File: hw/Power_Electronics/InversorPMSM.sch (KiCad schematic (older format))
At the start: 101 parts, among them J1 FROM_CONTROL_BOARD, Q1 HY1908D, Q10 JCS24N50WH, Q11 JCS24N50WH, Q12 JCS24N50WH, Q2 HY1908D, Q3 HY1908D, Q4 HY1908D, Q5 HY1908D, Q6 HY1908D, Q7 JCS24N50WH, Q8 JCS24N50WH, Q9 JCS24N50WH, U1 STDRIVE601

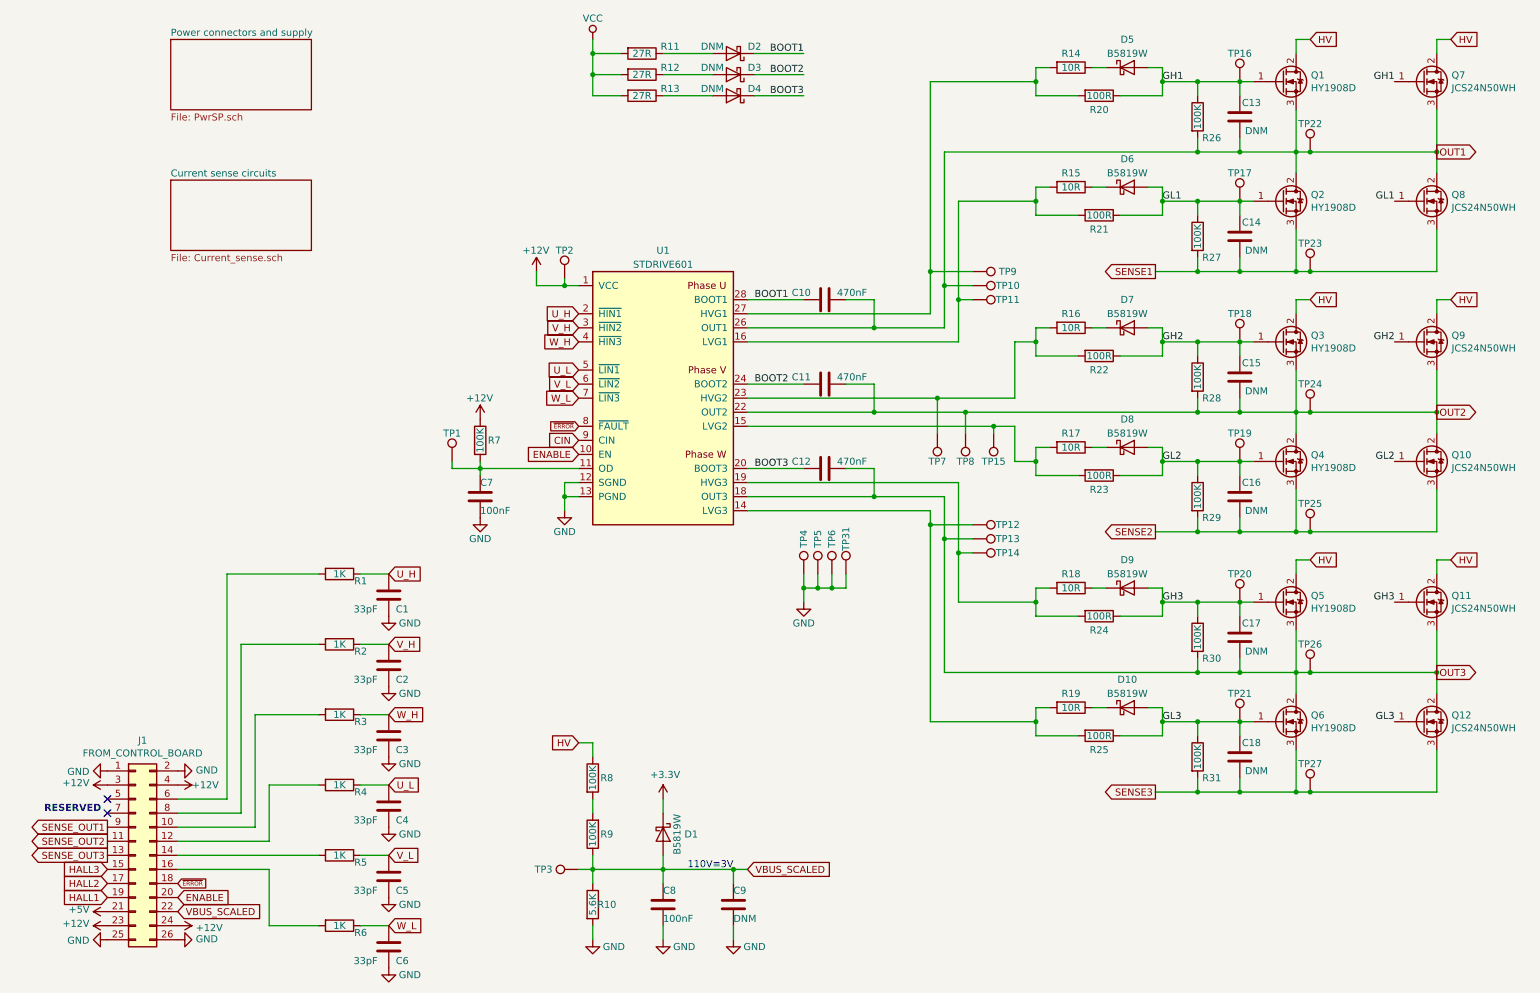
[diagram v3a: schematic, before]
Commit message: adjustments made on silkscreen layer
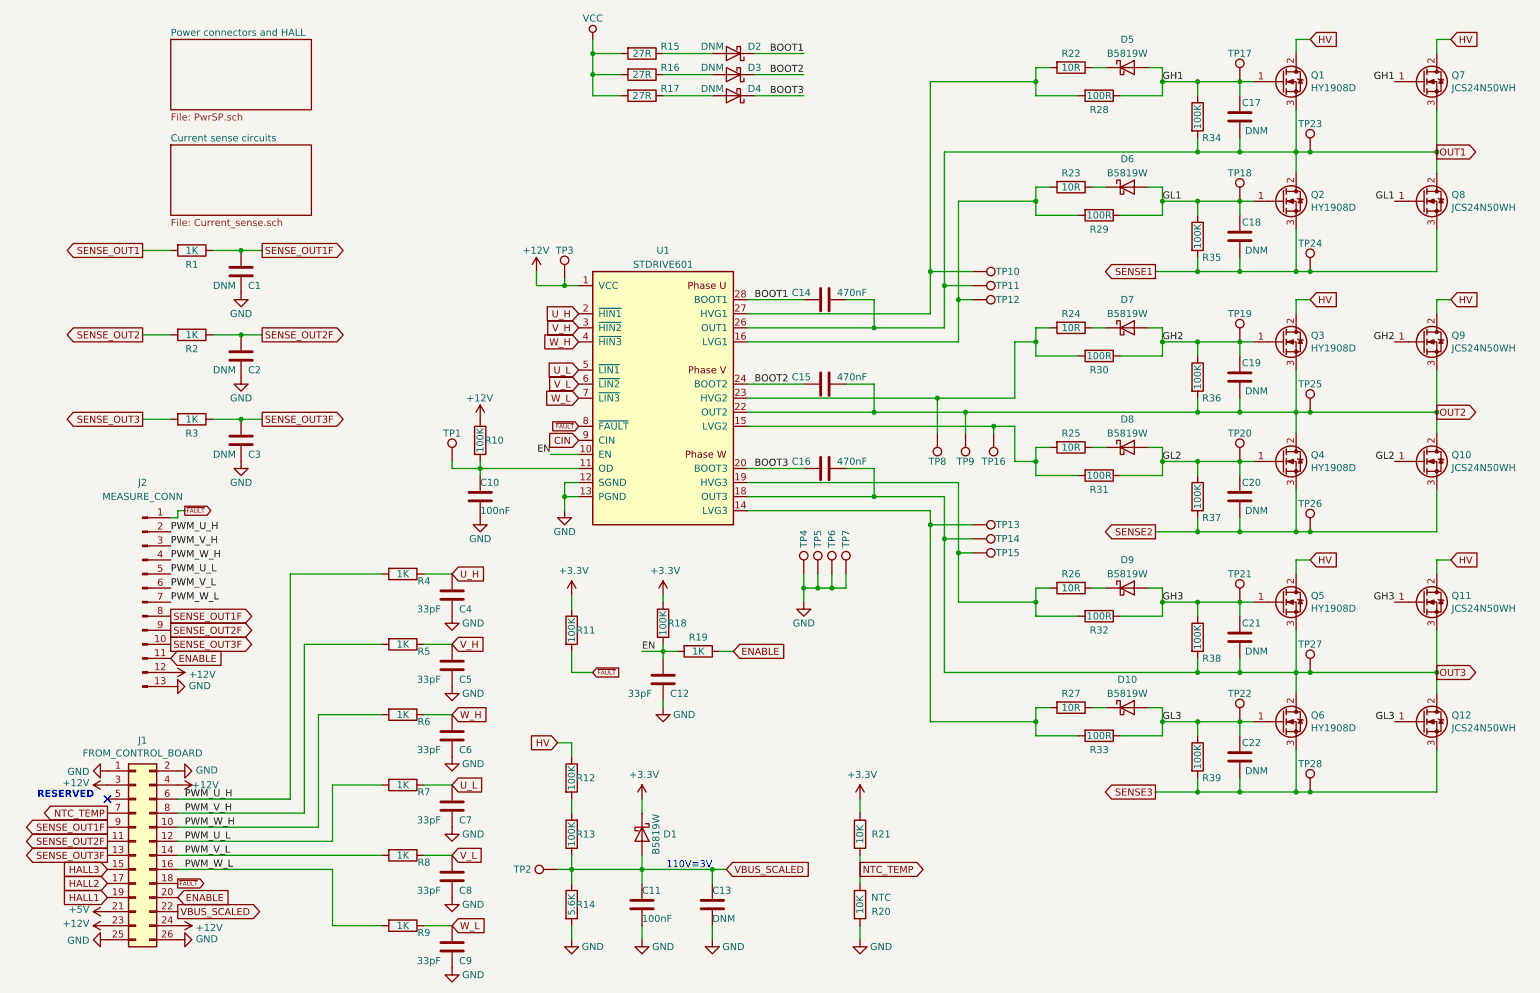
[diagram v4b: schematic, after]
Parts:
- added C1, C2, C3: DNM, Capacitor_SMD:C_0603_1608Metric, symbol Device:C
- added C12: 33pF, Capacitor_SMD:C_0603_1608Metric, symbol Device:C
- added J2: MEASURE_CONN, Connector_PinHeader_2.54mm:PinHeader_1x13_P2.54mm_Vertical, symbol Connector:Conn_01x13_Male
- added R1, R19, R2, R3: 1K, Resistor_SMD:R_0603_1608Metric, symbol Device:R
- added R11, R18: 100K, Resistor_SMD:R_0603_1608Metric, symbol Device:R
- added R20, R21: 10K, Resistor_SMD:R_0603_1608Metric, symbol Device:R
- renumbered C7 to C10, C8 to C11, C9 to C13, C10 to C14, C11 to C15, C12 to C16, C13 to C17, C14 to C18, C15 to C19, C16 to C20, C17 to C21, C18 to C22, C1 to C4, C2 to C5, C3 to C6, C4 to C7, C5 to C8, C6 to C9, R7 to R10, R8 to R12, R9 to R13, R10 to R14, R11 to R15, R12 to R16, R13 to R17, R14 to R22, R15 to R23, R16 to R24, R17 to R25, R18 to R26, R19 to R27, R20 to R28, R21 to R29, R22 to R30, R23 to R31, R24 to R32, R25 to R33, R26 to R34, R27 to R35, R28 to R36, R29 to R37, R30 to R38, R31 to R39, R1 to R4, R2 to R5, R3 to R6, R4 to R7, R5 to R8, R6 to R9, TP9 to TP10, TP10 to TP11, TP11 to TP12, TP12 to TP13, TP13 to TP14, TP14 to TP15, TP15 to TP16, TP16 to TP17, TP17 to TP18, TP18 to TP19, TP3 to TP2, TP19 to TP20, TP20 to TP21, TP21 to TP22, TP22 to TP23, TP23 to TP24, TP24 to TP25, TP25 to TP26, TP26 to TP27, TP27 to TP28, TP2 to TP3, TP31 to TP7, TP7 to TP8, TP8 to TP9
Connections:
- net +12V: now also J2.12 (Pin_12)
- net +3V3: now also R11.1, R18.1, R21.1
- net ENABLE: now also J2.11 (Pin_11), R19.1; no longer U1.10 (EN)
- net GND: now also C1.2, C12.2, C2.2, C3.2, J2.13 (Pin_13), R20.2
- net SENSE_OUT1: now also R1.2; no longer J1.9 (Pin_9)
- net SENSE_OUT2: now also R2.2; no longer J1.11 (Pin_11)
- net SENSE_OUT3: now also R3.2; no longer J1.13 (Pin_13)
- net PWM_W_L: now reaches J1.16 (Pin_16), R9.2
- net PWM_W_L: now also J2.7 (Pin_7)
- net PWM_V_L: now reaches J1.14 (Pin_14), R8.2
- net PWM_V_L: now also J2.6 (Pin_6)
- net PWM_U_L: now reaches J1.12 (Pin_12), R7.2
- net PWM_U_L: now also J2.5 (Pin_5)
- net PWM_W_H: now reaches J1.10 (Pin_10), R6.2
- net PWM_W_H: now also J2.4 (Pin_4)
- net PWM_V_H: now reaches J1.8 (Pin_8), R5.2
- net PWM_V_H: now also J2.3 (Pin_3)
- net PWM_U_H: now reaches J1.6 (Pin_6), R4.2
- net PWM_U_H: now also J2.2 (Pin_2)
- net NTC_TEMP: now reaches J1.7 (Pin_7)
- net NTC_TEMP: now also R20.1, R21.2
- net ~ERROR renamed ~FAULT
- net ~FAULT: now also J2.1 (Pin_1), R11.2
- new net EN: C12.1, R18.2, R19.2, U1.10 (EN)
- new net SENSE_OUT1F: C1.1, J1.9 (Pin_9), J2.8 (Pin_8), R1.1
- new net SENSE_OUT2F: C2.1, J1.11 (Pin_11), J2.9 (Pin_9), R2.1
- new net SENSE_OUT3F: C3.1, J1.13 (Pin_13), J2.10 (Pin_10), R3.1
- no-connect marks 2 -> 1
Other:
- moved on the sheet: C11, C13, C4, C5, C6, C7, C8, C9, D1, R12, R13, R14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

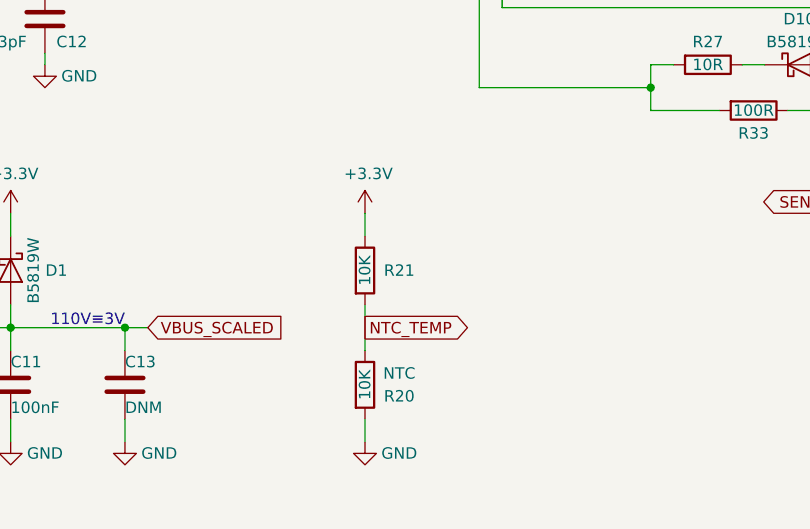
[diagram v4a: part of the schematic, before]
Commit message: turn power electronics PCB into a 2 layer board
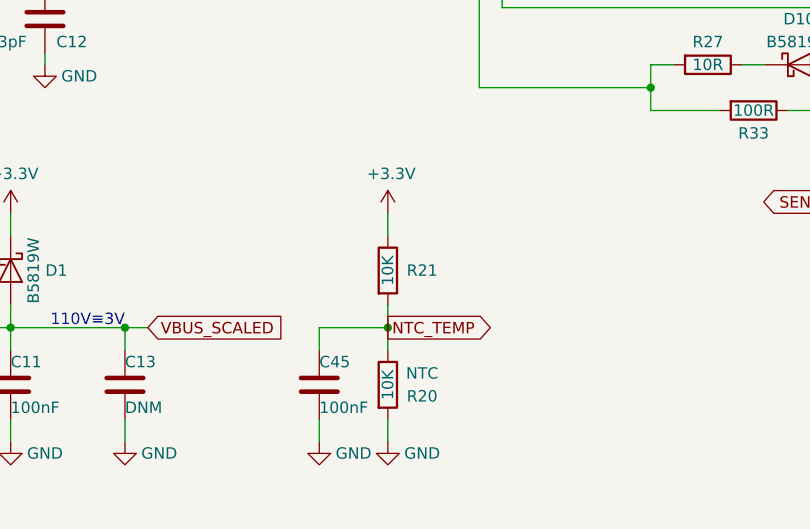
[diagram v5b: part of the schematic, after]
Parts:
- added C45: 100nF, Capacitor_SMD:C_0603_1608Metric, symbol Device:C
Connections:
- net GND: now also C45.2
- net NTC_TEMP: now also C45.1
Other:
- moved on the sheet: R20, R21
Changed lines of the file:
@@
 L power:+3.3V #PWR?
 U 1 1 6047BC31
-P 6400 6400
+P 6500 6400
 AR Path="/6028AEA0/6047BC31" Ref="#PWR?"  Part="1"
 AR Path="/6047BC31" Ref="#PWR034"  Part="1"
-F 0 "#PWR034" H 6400 6250 50  0001 C CNN
-F 1 "+3.3V" H 6415 6573 50  0000 C CNN
-F 2 "" H 6400 6400 50  0001 C CNN
-F 3 "" H 6400 6400 50  0001 C CNN
-	1    6400 6400
+F 0 "#PWR034" H 6500 6250 50  0001 C CNN
+F 1 "+3.3V" H 6515 6573 50  0000 C CNN
+F 2 "" H 6500 6400 50  0001 C CNN
+F 3 "" H 6500 6400 50  0001 C CNN
+	1    6500 6400
 	1    0    0    -1
 $EndComp
@@
 L Device:R R21
 U 1 1 604A0052
-P 6400 6650
+P 6500 6650
 AR Path="/604A0052" Ref="R21"  Part="1"
 AR Path="/6016C275/604A0052" Ref="R?"  Part="1"
-F 0 "R21" H 6550 6650 50  0000 C CNN
-F 1 "10K" V 6400 6650 50  0000 C CNN
-F 2 "Resistor_SMD:R_0603_1608Metric" V 6330 6650 50  0001 C CNN
-F 3 "" H 6400 6650 50  0001 C CNN
-F 4 "C25804" V 6400 6650 50  0001 C CNN "LCSC"
-	1    6400 6650
+F 0 "R21" H 6650 6650 50  0000 C CNN
+F 1 "10K" V 6500 6650 50  0000 C CNN
+F 2 "Resistor_SMD:R_0603_1608Metric" V 6430 6650 50  0001 C CNN
+F 3 "" H 6500 6650 50  0001 C CNN
+F 4 "C25804" V 6500 6650 50  0001 C CNN "LCSC"
+	1    6500 6650
 	1    0    0    -1
 $EndComp
@@
 L power:GND #PWR035
 U 1 1 604A0684
-P 6400 7400
-F 0 "#PWR035" H 6400 7150 50  0001 C CNN
-F 1 "GND" H 6550 7350 50  0000 C CNN
-F 2 "" H 6400 7400 50  0001 C CNN
-F 3 "" H 6400 7400 50  0001 C CNN
-	1    6400 7400
-	1    0    0    -1
-$EndComp
-Wire Wire Line
-	6400 6400 6400 6500
-Wire Wire Line
-	6400 6800 6400 7000
-Wire Wire Line
-	6400 7300 6400 7400
+P 6500 7400
+F 0 "#PWR035" H 6500 7150 50  0001 C CNN
+F 1 "GND" H 6650 7350 50  0000 C CNN
+F 2 "" H 6500 7400 50  0001 C CNN
+F 3 "" H 6500 7400 50  0001 C CNN
+	1    6500 7400
+	1    0    0    -1
+$EndComp
+Wire Wire Line
+	6500 6400 6500 6500
+Wire Wire Line
+	6500 6800 6500 6900
+Wire Wire Line
+	6500 7300 6500 7400
 $Comp
 L Device:R R20
 U 1 1 60486FFF
-P 6400 7150
+P 6500 7150
 AR Path="/60486FFF" Ref="R20"  Part="1"
 AR Path="/6016C275/60486FFF" Ref="R?"  Part="1"
-F 0 "R20" H 6550 7100 50  0000 C CNN
-F 1 "10K" V 6400 7150 50  0000 C CNN
-F 2 "Resistor_SMD:R_0603_1608Metric" V 6330 7150 50  0001 C CNN
-F 3 "" H 6400 7150 50  0001 C CNN
-F 4 "C13564" V 6400 7150 50  0001 C CNN "LCSC"
-F 5 "NTC" H 6550 7200 50  0000 C CNN "Comments"
-	1    6400 7150
-	1    0    0    -1
-$EndComp
-Text GLabel 6400 6900 2    50   Output ~ 0
+F 0 "R20" H 6650 7100 50  0000 C CNN
+F 1 "10K" V 6500 7150 50  0000 C CNN
+F 2 "Resistor_SMD:R_0603_1608Metric" V 6430 7150 50  0001 C CNN
+F 3 "" H 6500 7150 50  0001 C CNN
+F 4 "C13564" V 6500 7150 50  0001 C CNN "LCSC"
+F 5 "NTC" H 6650 7200 50  0000 C CNN "Comments"
+	1    6500 7150
+	1    0    0    -1
+$EndComp
+Text GLabel 6500 6900 2    50   Output ~ 0
 NTC_TEMP
 Text GLabel 1050 6500 0    50   Output ~ 0
@@
 Text GLabel 1500 5100 2    50   Output ~ 0
 SENSE_OUT1F
+$Comp
+L Device:C C?
+U 1 1 5FF66380
+P 6200 7150
+AR Path="/6028AEA0/5FF66380" Ref="C?"  Part="1"
+AR Path="/5FF66380" Ref="C45"  Part="1"
+F 0 "C45" H 6200 7250 50  0000 L CNN
+F 1 "100nF" H 6200 7050 50  0000 L CNN
+F 2 "Capacitor_SMD:C_0603_1608Metric" H 6238 7000 50  0001 C CNN
+F 3 "~" H 6200 7150 50  0001 C CNN
+F 4 "C14663" H 6200 7150 50  0001 C CNN "LCSC"
+	1    6200 7150
+	1    0    0    -1
+$EndComp
+$Comp
+L power:GND #PWR0101
+U 1 1 5FFA37C4
+P 6200 7400
+F 0 "#PWR0101" H 6200 7150 50  0001 C CNN
+F 1 "GND" H 6350 7350 50  0000 C CNN
+F 2 "" H 6200 7400 50  0001 C CNN
+F 3 "" H 6200 7400 50  0001 C CNN
+	1    6200 7400
+	1    0    0    -1
+$EndComp
+Wire Wire Line
+	6200 7400 6200 7300
+Wire Wire Line
+	6200 7000 6200 6900
+Wire Wire Line
+	6200 6900 6500 6900
+Connection ~ 6500 6900
+Wire Wire Line
+	6500 6900 6500 7000
 $EndSCHEMATC

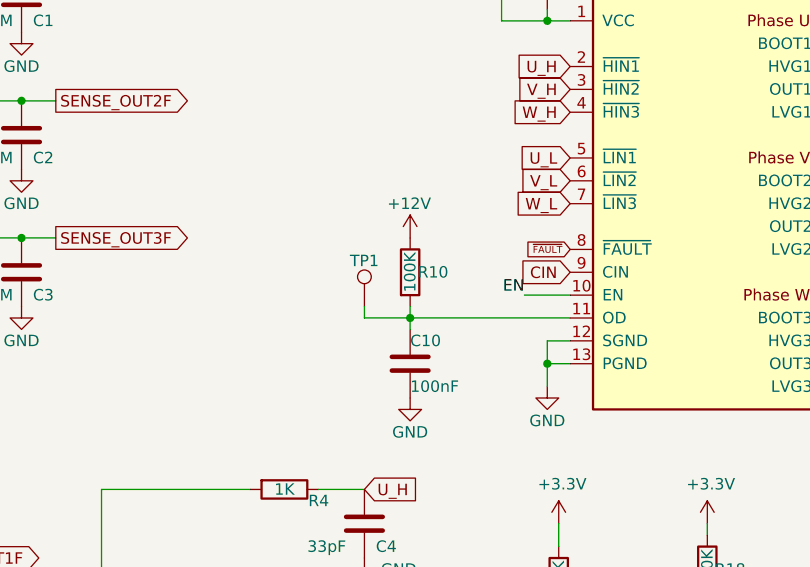
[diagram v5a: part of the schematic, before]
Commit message: adjusts made on mask layer to expose high current path
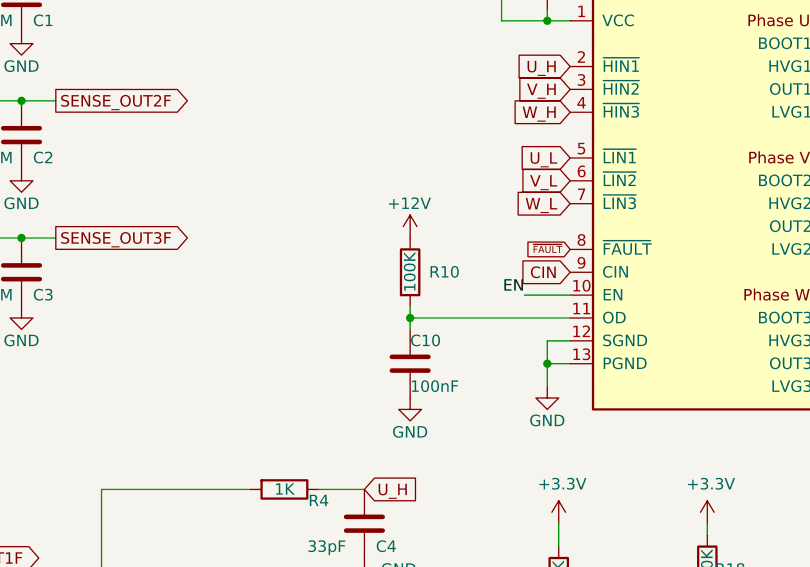
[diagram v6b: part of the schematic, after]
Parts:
- removed TP1: TestPoint, TestPoint:TestPoint_Pad_D1.5mm, symbol Connector:TestPoint
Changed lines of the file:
@@
 U 1 1 606C280C
 P 3700 3850
-F 0 "R10" H 3800 3850 50  0000 C CNN
+F 0 "R10" H 3850 3850 50  0000 C CNN
 F 1 "100K" V 3700 3850 50  0000 C CNN
 F 2 "Resistor_SMD:R_0603_1608Metric" V 3630 3850 50  0001 C CNN
@@
 	1    0    0    -1
 $EndComp
-$Comp
-L Connector:TestPoint TP1
-U 1 1 60708132
-P 3500 4000
-F 0 "TP1" H 3500 4200 50  0000 C CNN
-F 1 "TestPoint" H 3558 4027 50  0001 L CNN
-F 2 "TestPoint:TestPoint_Pad_D1.5mm" H 3700 4000 50  0001 C CNN
-F 3 "~" H 3700 4000 50  0001 C CNN
-	1    3500 4000
-	1    0    0    -1
-$EndComp
-Wire Wire Line
-	3500 4000 3500 4050
-Wire Wire Line
-	3500 4050 3700 4050
 Text GLabel 10500 1800 2    50   Output ~ 0
 OUT1
